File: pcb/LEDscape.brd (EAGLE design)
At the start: 71.8 x 54.6 mm, 41 parts, among them IC1 MAX3040CSE, IC2 MAX3040CSE, IC3 MAX3040CSE, IC4 MAX3040CSE, IC5 MAX3040CSE, IC6 MAX3040CSE, IC7 MAX3040CSE, IC8 MAX3040CSE

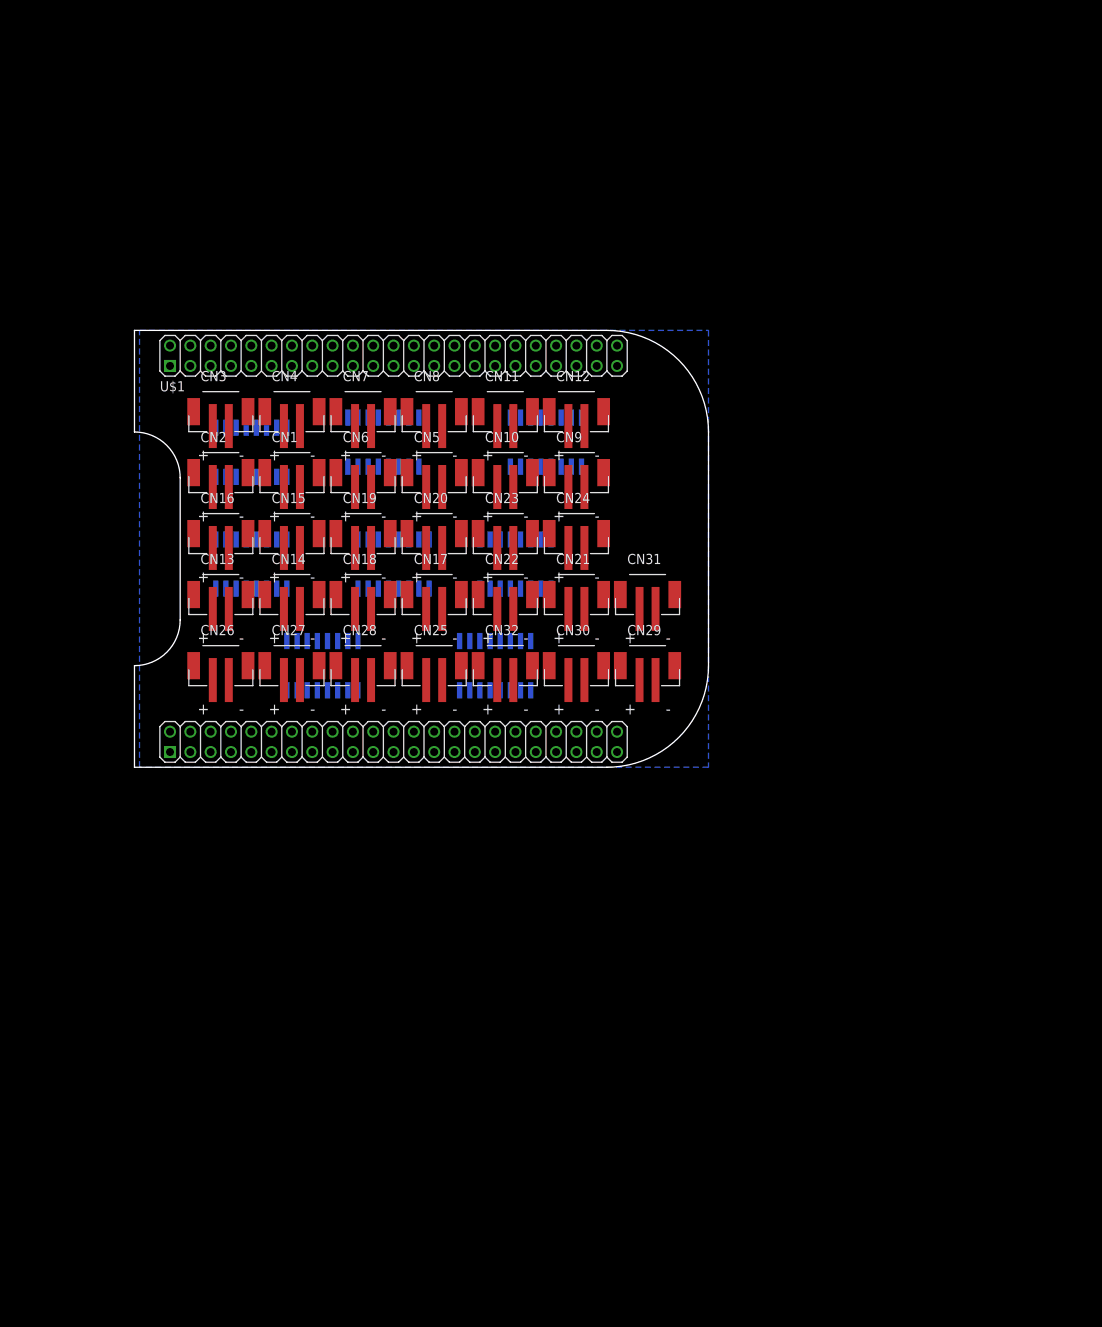
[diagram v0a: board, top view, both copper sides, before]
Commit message: Update board to use 2x8 RJ45 connector
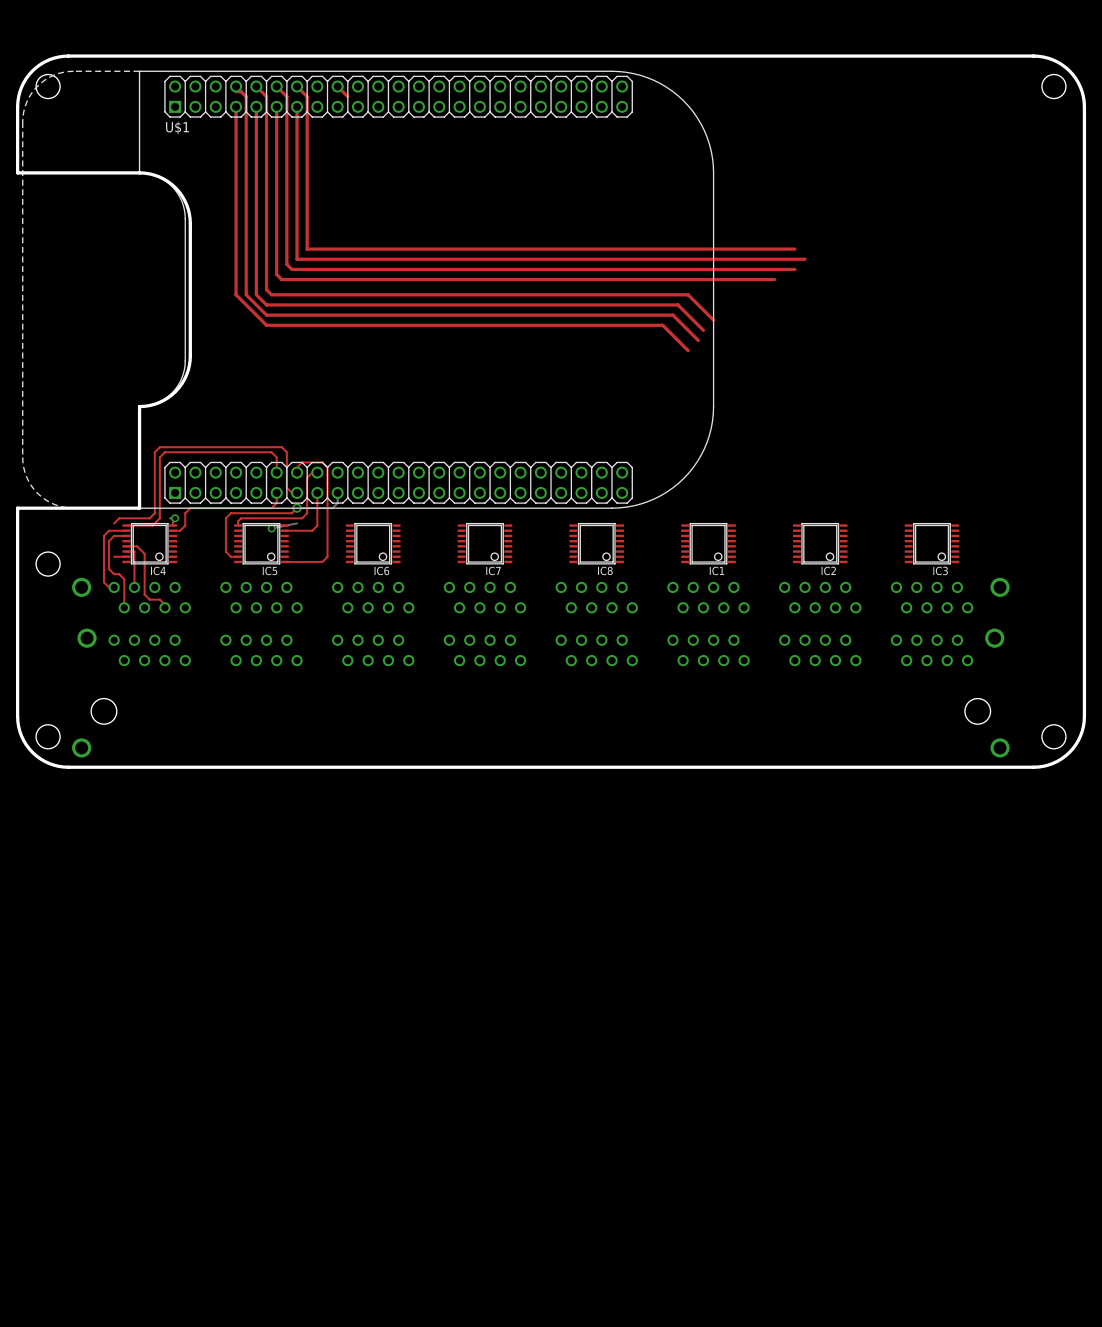
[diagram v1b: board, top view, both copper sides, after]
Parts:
- removed CN1, CN10, CN11, CN12, CN13, CN14, CN15, CN16, CN17, CN18, CN19, CN2, CN20, CN21, CN22, CN23, CN24, CN25, CN26, CN27, CN28, CN29, CN3, CN30, CN31, CN32, CN4, CN5, CN6, CN7, CN8, CN9: (no value), adafruit:JST-PH-2-SMT
- added U$10, U$3, U$4, U$5, U$6, U$7, U$8, U$9: RJ45_8X2_JACK, LEDscape:RJ45_8X2_JACK
- added U$2: RJ45_8X2_BASE, LEDscape:RJ45_8X2_BASE
- IC1, IC2, IC3, IC4, IC5, IC6, IC7, IC8: value MAX3040CSE -> MAX3041CUE; device maxim:SO16 -> maxim:TSSOP16
- U$1: value BEAGLEBONE_OUTLINE -> BEAGLEBONE_NO_OUTLINE; device adafruit:BEAGLEBONE_SHIELD -> LEDscape:BEAGLEBONE_SHIELD_NO_OUTLINE
- moved IC1 58.3 mm to (86.4, 27.9), flipped to the top, turned to 90 degrees
- moved IC2 56.1 mm to (100.3, 27.9), flipped to the top, turned to 90 degrees
- moved IC3 49.9 mm to (114.3, 27.9), flipped to the top, turned to 90 degrees
- moved U$1 32.4 mm to (0.64, 87.0)
- moved IC7 25.4 mm to (58.4, 27.9), flipped to the top, turned to 90 degrees
- moved IC8 19.8 mm to (72.4, 27.9), flipped to the top, turned to 90 degrees
- moved IC6 18.0 mm to (44.5, 27.9), flipped to the top, turned to 90 degrees
- moved IC5 16.7 mm to (30.5, 27.9), flipped to the top, turned to 90 degrees
- moved IC4 13.0 mm to (16.5, 27.9), flipped to the top, turned to 90 degrees
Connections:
- removed net N$57: CN28.2, IC7.14
- removed net N$66: CN32.1, IC8.13
- new net N$11: IC6.5, U$7.6
- new net N$14: IC3.5, U$5.6
- net GND: now also U$10.15, U$10.16, U$10.7, U$10.8, U$3.15, U$3.16, U$3.7, U$3.8, U$4.15, U$4.16, U$4.7, U$4.8, U$5.15, U$5.16, U$5.7, U$5.8, U$6.15, U$6.16, U$6.7, U$6.8, U$7.15, U$7.16, U$7.7, U$7.8, U$8.15, U$8.16, U$8.7, U$8.8, U$9.15, U$9.16, U$9.7, U$9.8
- net N$1: now also U$3.1; no longer CN1.2
- net N$10: now also U$4.2; no longer CN5.1
- net N$12: now also U$4.3; no longer CN6.2
- net N$13: now also U$4.6; no longer CN6.1
- net N$15: now also U$4.9; no longer CN7.2
- net N$16: now also U$4.10; no longer CN7.1
- net N$17: now also U$4.11; no longer CN8.2
- net N$18: now also U$4.14; no longer CN8.1
- net N$19: now also U$5.1; no longer CN9.2
- net N$2: now also U$3.2; no longer CN1.1
- net N$20: now also U$5.2; no longer CN9.1
- net N$21: now also U$5.3; no longer CN10.2
- net N$22: now also IC3.13, U$5.14; no longer CN10.1, IC3.5
- net N$23: now also U$5.9; no longer CN11.2
- net N$24: now also U$5.10; no longer CN11.1
- net N$25: now also U$5.11; no longer CN12.2
- net N$26: now also IC7.6, U$8.3; no longer CN12.1, IC3.13
- net N$27: now also U$9.1; no longer CN13.2
- net N$28: now also U$9.2; no longer CN13.1
- net N$29: now also U$9.3; no longer CN14.2
- net N$3: now also U$4.1; no longer CN5.2
- net N$30: now also U$9.6; no longer CN14.1
- net N$31: now also IC4.13, U$9.14; no longer CN15.2, IC4.10
- net N$32: now also U$9.10; no longer CN15.1
- net N$33: now also U$9.11; no longer CN16.2
- net N$34: now also IC4.10, U$9.9; no longer CN16.1, IC4.13
- net N$35: now also U$6.1; no longer CN17.2
- net N$36: now also U$6.2; no longer CN17.1
- net N$37: now also U$6.3; no longer CN18.2
- net N$38: now also U$6.6; no longer CN18.1
- net N$39: now also U$6.9; no longer CN19.2
- net N$4: now also U$3.3; no longer CN2.2
- net N$40: now also U$6.10; no longer CN19.1
- net N$41: now also U$6.11; no longer CN20.2
- net N$42: now also U$6.14; no longer CN20.1
- net N$43: now also U$7.1; no longer CN21.2
- net N$44: now also U$7.2; no longer CN21.1
- net N$45: now also U$7.3; no longer CN22.2
- net N$46: now also IC7.5, U$8.6; no longer CN22.1, IC6.5
- net N$47: now also U$7.9; no longer CN23.2
- net N$48: now also U$7.10; no longer CN23.1
- net N$49: now also U$7.11; no longer CN24.2
- net N$5: now also U$3.6; no longer CN2.1
- net N$50: now also U$7.14; no longer CN24.1
- net N$51: now also U$8.1; no longer CN25.2
- net N$52: now also U$8.2; no longer CN25.1
- net N$53: now also IC7.10, U$8.9; no longer CN26.2, IC7.6
- net N$54: now also IC7.14, U$8.11; no longer CN26.1, IC7.5
- net N$55: now also IC7.13, U$8.14; no longer CN27.2, IC7.10
- net N$56: now also U$8.10; no longer CN27.1
- net N$58: now also IC8.6, U$10.3; no longer CN28.1, IC7.13
- net N$59: now also U$10.1; no longer CN29.2
- net N$6: now also U$3.9; no longer CN3.2
- net N$60: now also U$10.2; no longer CN29.1
- net N$61: now also IC8.5, U$10.6; no longer CN30.2, IC8.6
- net N$62: now also IC8.14, U$10.11; no longer CN30.1, IC8.5
- net N$63: now also U$10.9; no longer CN31.2
- net N$64: now also U$10.10; no longer CN31.1
- net N$65: now also IC8.13, U$10.14; no longer CN32.2, IC8.14
- net N$7: now also U$3.10; no longer CN3.1
- net N$8: now also U$3.11; no longer CN4.2
- net N$9: now also U$3.14; no longer CN4.1
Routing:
- net S5: track 0.00 -> 86.5 mm
- net S1: track 0.00 -> 85.8 mm
- net S4: track 0.00 -> 83.4 mm
- net S3: track 0.00 -> 83.4 mm
- net S0: track 0.00 -> 82.9 mm
- net S6: track 0.00 -> 82.5 mm
- net S7: track 0.00 -> 81.8 mm
- net S2: track 0.00 -> 81.2 mm
- net S15: track 0.00 -> 37.8 mm
- net S14: track 0.00 -> 29.2 mm
- net S19: track 0.00 -> 22.0 mm, vias 0 -> 1
- net S16: track 0.00 -> 21.7 mm
- net S13: track 0.00 -> 16.6 mm
- net S18: track 0.00 -> 15.6 mm
- net N$32: track 0.00 -> 11.9 mm
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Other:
- board size 71.8 x 54.6 mm -> 133.3 x 88.9 mm

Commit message: Flip board over (put everything on the front, not the back), add caps, work on routing.
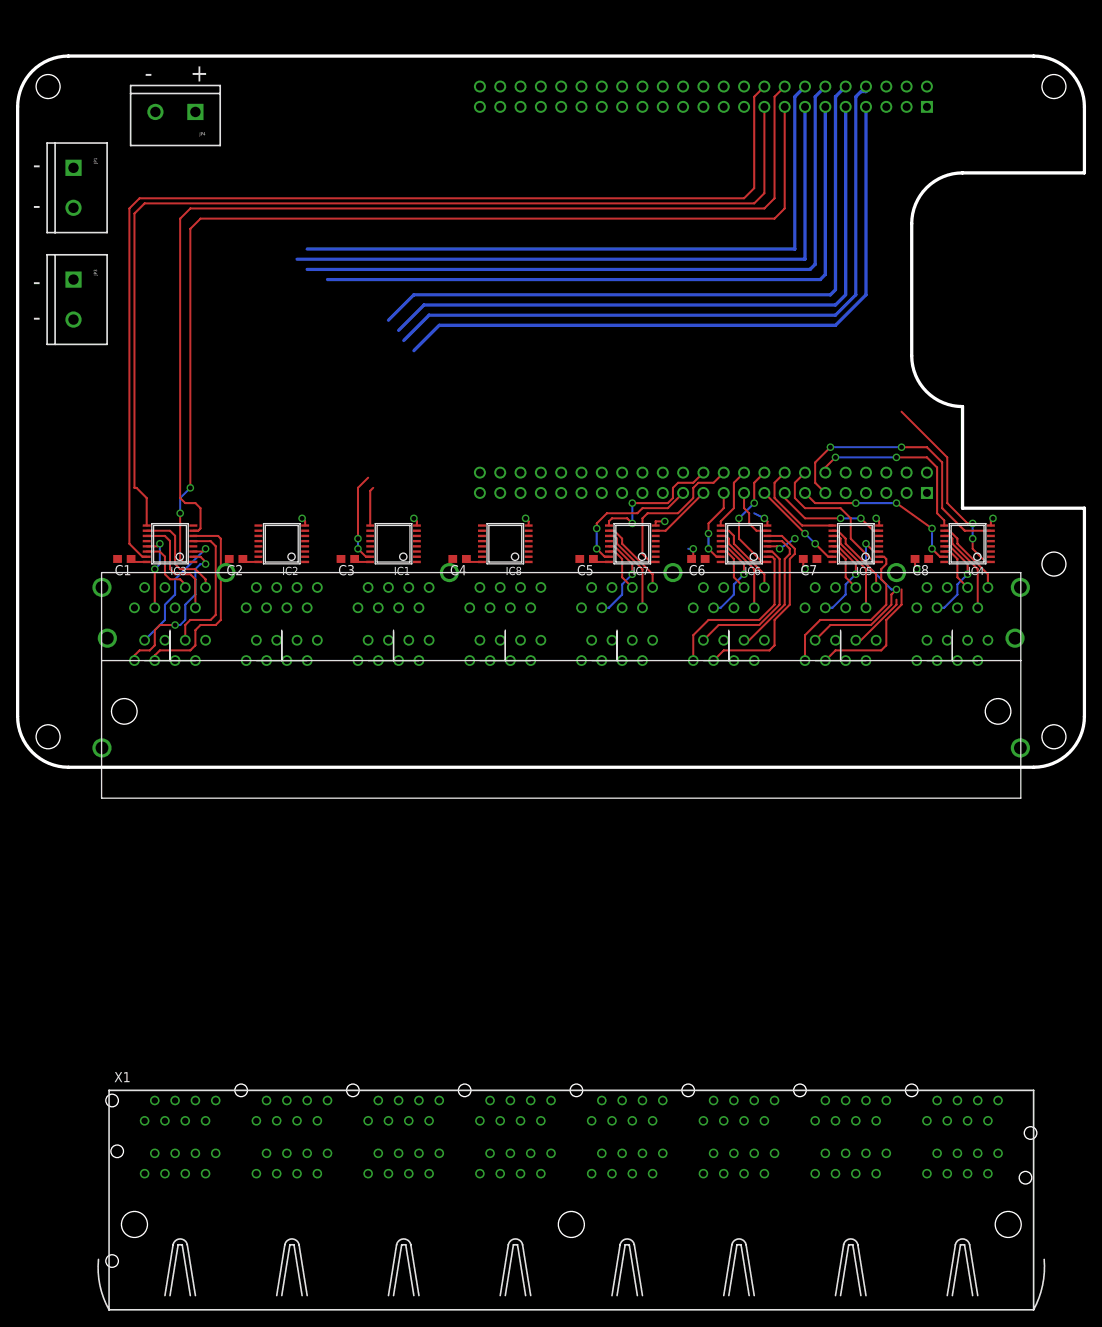
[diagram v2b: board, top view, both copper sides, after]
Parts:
- added C1, C2, C3, C4, C5, C6, C7, C8: .1uF, adafruit:C0603
- added JP1, JP3, JP4: (no value), SparkFun-Connectors:SCREWTERMINAL-5MM-2
- added X1: 44520-0003, con-molex:44520-0003
- moved U$1 132.1 mm to (132.7, 87.0), flipped to the bottom
- moved IC4 102.2 mm to (118.7, 27.9)
- moved U$9 100.3 mm to (116.8, 13.3), flipped to the top
- moved IC3 95.2 mm to (19.1, 27.9)
- moved U$5 95.2 mm to (19.1, 13.3), flipped to the top
- moved IC5 74.3 mm to (104.8, 27.9)
- moved U$6 72.4 mm to (102.9, 13.3), flipped to the top
- moved IC2 67.3 mm to (33.0, 27.9)
- moved U$4 67.3 mm to (33.0, 13.3), flipped to the top
- moved IC6 46.4 mm to (90.8, 27.9)
- moved U$7 44.5 mm to (88.9, 13.3), flipped to the top
- moved IC1 39.4 mm to (47.0, 27.9)
- moved U$3 39.4 mm to (47.0, 13.3), flipped to the top
- moved IC7 18.4 mm to (76.8, 27.9)
- moved U$8 16.5 mm to (74.9, 13.3), flipped to the top
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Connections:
- net +5V: now also C1.1, C2.1, C3.1, C4.1, C5.1, C6.1, C7.1, C8.1, JP4.1
- net GND: now also C1.2, C2.2, C3.2, C4.2, C5.2, C6.2, C7.2, C8.2, JP1.1, JP1.2, JP3.1, JP3.2, JP4.2
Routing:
- net S11: track 1.80 -> 137.1 mm
- net S8: track 0.00 -> 131.6 mm, vias 0 -> 2
- net S9: track 0.00 -> 131.4 mm
- net S10: track 0.00 -> 130.4 mm
- net N$45: track 0.00 -> 25.7 mm
- net N$21: track 0.00 -> 25.6 mm
- net S12: track 0.00 -> 24.2 mm, vias 0 -> 2
- net N$36: track 0.00 -> 23.3 mm, vias 0 -> 2
- net N$35: track 0.00 -> 22.2 mm
- net N$43: track 0.00 -> 21.6 mm
- net N$19: track 0.00 -> 20.4 mm, vias 0 -> 2
- net S24: track 0.00 -> 19.8 mm
- net N$44: track 0.00 -> 19.0 mm
- net S13: track 16.6 -> 34.8 mm, vias 0 -> 2
- net N$14: track 0.00 -> 17.9 mm
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- added copper zone on layer 1, net +5V
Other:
- outline, holes or cut-outs redrawn
- board text added: "+"
- board text added: "-"

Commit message: Fully routed, 8mil clearances, 10mil minimum traces
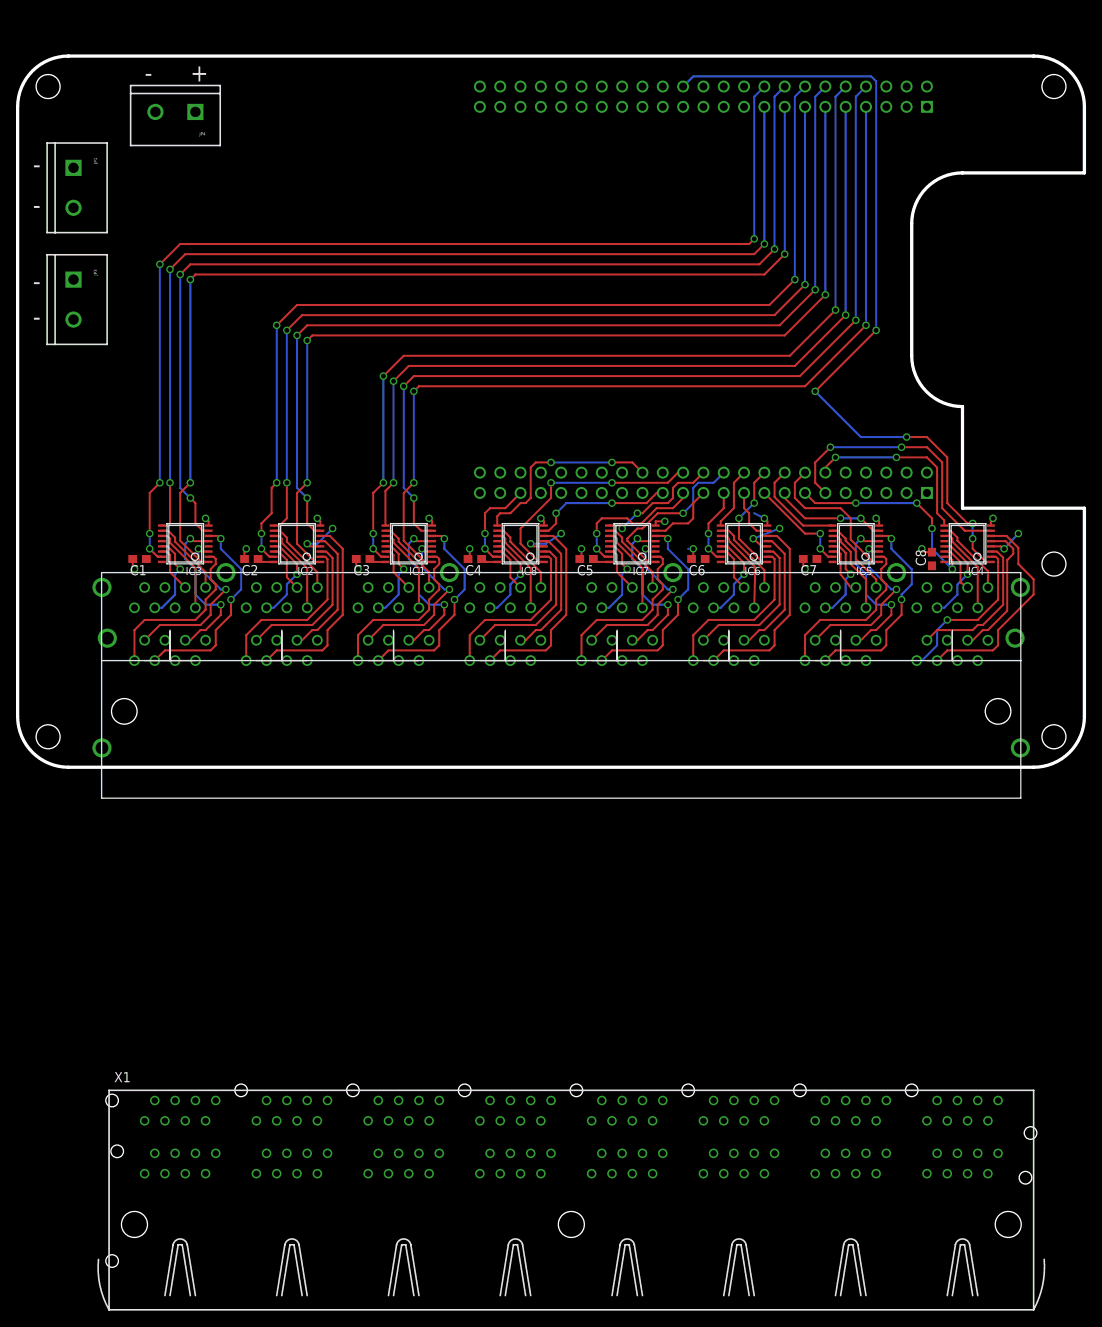
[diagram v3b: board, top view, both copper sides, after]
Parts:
- moved C2 1.91 mm to (29.2, 26.0)
- moved C3 1.91 mm to (43.2, 26.0)
- moved C4 1.91 mm to (57.1, 26.0)
- moved IC1 1.91 mm to (48.9, 27.9)
- moved IC8 1.91 mm to (62.9, 27.9)
- moved C1 1.90 mm to (15.2, 26.0)
- moved IC3 1.90 mm to (21.0, 27.9)
- moved IC2 1.90 mm to (34.9, 27.9)
- moved C8 1.27 mm to (114.3, 26.0), turned to 90 degrees
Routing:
- net S12: track 24.2 -> 102.8 mm, vias 2 -> 5
- net S7: track 81.8 -> 122.5 mm, vias 0 -> 5
- net S4: track 83.4 -> 120.4 mm, vias 0 -> 3
- net S5: track 86.5 -> 119.1 mm, vias 0 -> 3
- net S6: track 82.5 -> 114.9 mm, vias 0 -> 3
- net S28: track 0.00 -> 30.1 mm, vias 0 -> 2
- net S0: track 82.9 -> 111.1 mm, vias 0 -> 3
- net N$29: track 0.00 -> 27.3 mm
- net N$4: track 0.00 -> 25.8 mm, vias 0 -> 2
- net N$26: track 0.00 -> 25.8 mm, vias 0 -> 2
- net S30: track 0.00 -> 24.9 mm, vias 0 -> 2
- net N$12: track 0.00 -> 24.7 mm
- net N$58: track 0.00 -> 24.7 mm
- net S1: track 85.8 -> 110.0 mm, vias 0 -> 3
- net N$52: track 0.00 -> 21.8 mm, vias 0 -> 2
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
